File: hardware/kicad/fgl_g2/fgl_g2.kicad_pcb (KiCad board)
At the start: 2 copper layers, 90 x 60 mm, 73 parts, among them J1 USB-C (from bank), J10 XIAO socket 8-14, J2 POT 100k lin + SW, J3 LD2410S socket, J4 LD2410S cable, J5 PORT 1, J6 PORT 2, J7 PORT 3, J8 PORT 4, J9 XIAO socket 1-7, Q1 AO3400A, Q2 AO3401A, U2 TPS61500PWPR

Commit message: G2: act on Flux's schematic review
- Section 2 (SEPIC) redrawn with wires instead of a label on every pin;
  one label per net, labels only where nets leave the section
- Label overlaps cleared: GND at JP1/JP2, VBUS_IN power flag, F1/Q2
  reference and value
- Silkscreen: "Remove shunt to flash" under the JP2 legend (GPIO8 low
  blocks download boot); same instruction in the flashing step
- G2-T6: scope the XIAO 5V pin (limit 6.0 V, XC6210) in both plug
  orientations; D1 cannot hold that, so a failure means an input OVP
  cut-off in G3. G2-T12: try a USB flash with the JP2 shunt on
- docs/g2_flux_schematic_review.md: Flux's findings with resolutions

KiCad netlist identical (nets, names, parts, fields); verify_netlist
passes; ERC 0 errors; DRC same 71 warnings; only F_Silkscreen.gto
changed among the gerbers; position file identical.

Co-Authored-By: Claude Opus 5.5 <noreply@anthropic.com>
Claude-Session: https://claude.ai/code/session_013HVPKWJHmpHbXpMbmhYHhv
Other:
- board text added: "Remove shunt to flash"
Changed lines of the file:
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@@
+		)
+	)
+	(gr_text "Remove shunt to flash"
+		(at 125.4 133.4 0)
+		(layer "F.SilkS")
+		(effects
+			(font
+				(size 0.8 0.8)
+				(thickness 0.12)
+			)
+			(justify left)
 		)
 	)

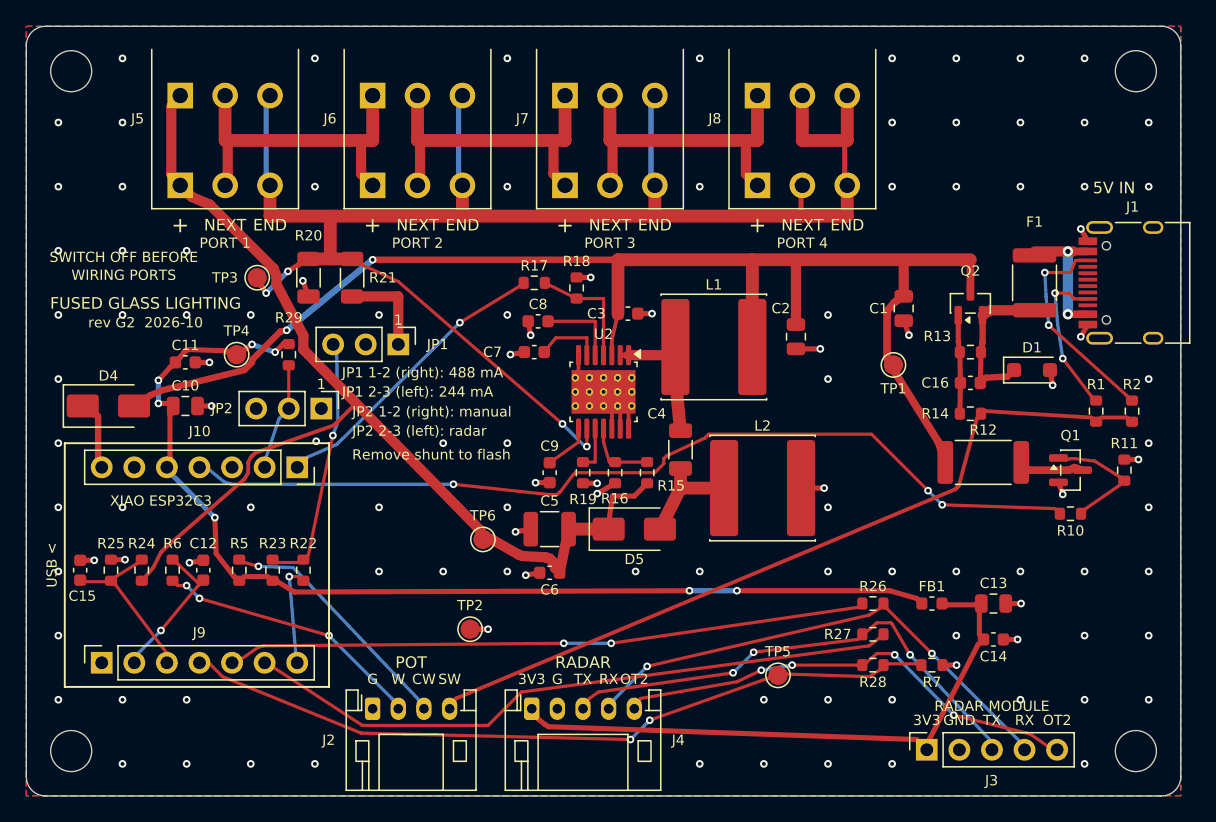
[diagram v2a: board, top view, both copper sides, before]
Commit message: G2: act on Flux's layout review: tighter switching loop, J1 vias off the shield
C4 under L1, D5 vertical below C4, C5/C6 beside D5's cathode over solid
B.Cu ground: loop area about 74 -> 52 mm^2. Router keeps vias 0.25 mm from
through-hole pads too, which moves J1's GND vias from 0.12 to 0.35 mm off
the shield pads. DRC 0 errors / 0 unconnected; verify_pcb passes; netlist
and BOM unchanged. Fab files, CPL, assembly drawing, renders regenerated.
Flux's review saved with a resolution for each finding.

Co-Authored-By: Claude Opus 5.5 <noreply@anthropic.com>
Claude-Session: https://claude.ai/code/session_013HVPKWJHmpHbXpMbmhYHhv
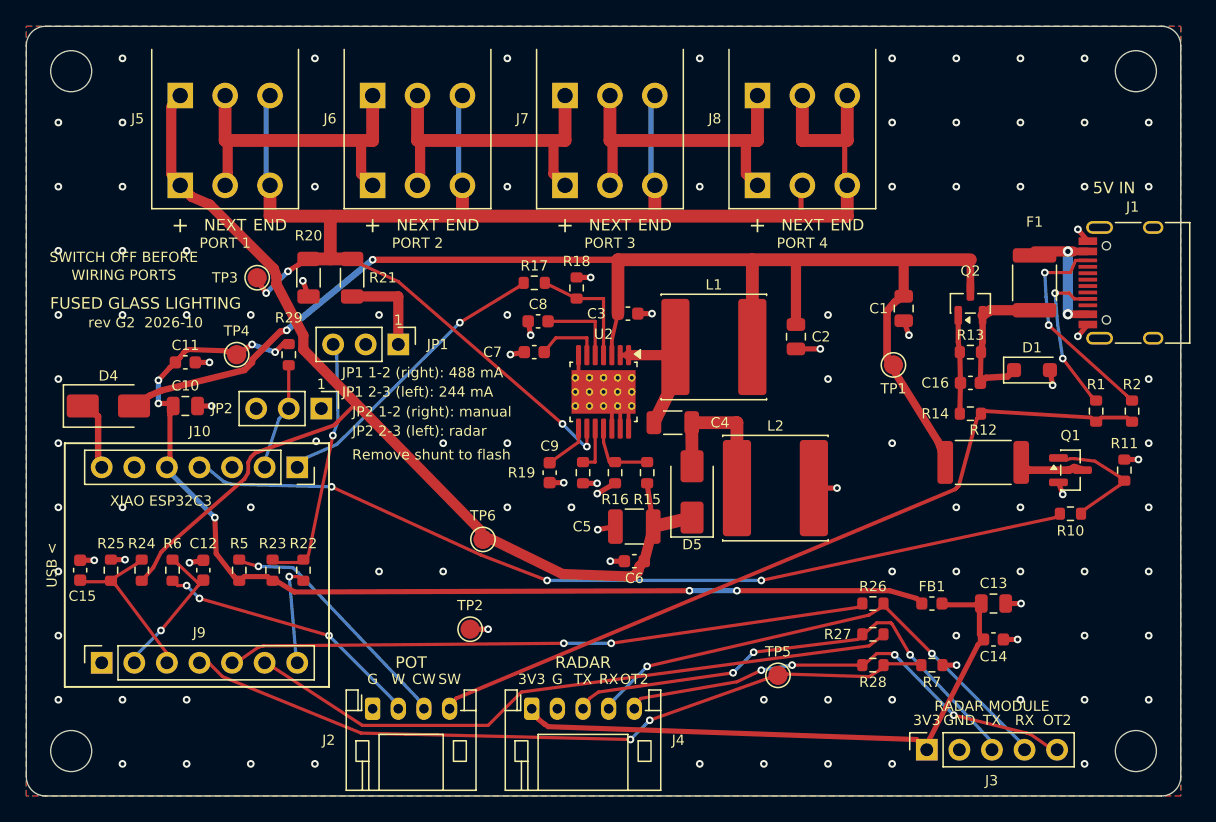
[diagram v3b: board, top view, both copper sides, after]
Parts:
- moved C6 6.66 mm to (147.4, 141.7)
- moved C5 6.60 mm to (147.4, 139.0)
- moved D5 5.35 mm to (151.9, 136.3), turned to 90 degrees
- moved C4 2.18 mm to (150.4, 130.9), turned to 0 degrees
- moved L2 1.00 mm to (158.4, 136.0)
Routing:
- net /VOUT: track 86.0 -> 90.4 mm
- net /KA_DRV: track 72.0 -> 69.6 mm
- net /SEP_B: track 8.50 -> 9.03 mm
- net GND: track 38.1 -> 38.5 mm, vias 111 -> 109
